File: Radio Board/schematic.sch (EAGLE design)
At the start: 3 parts, among them U1 XBP9X-DMRS-001

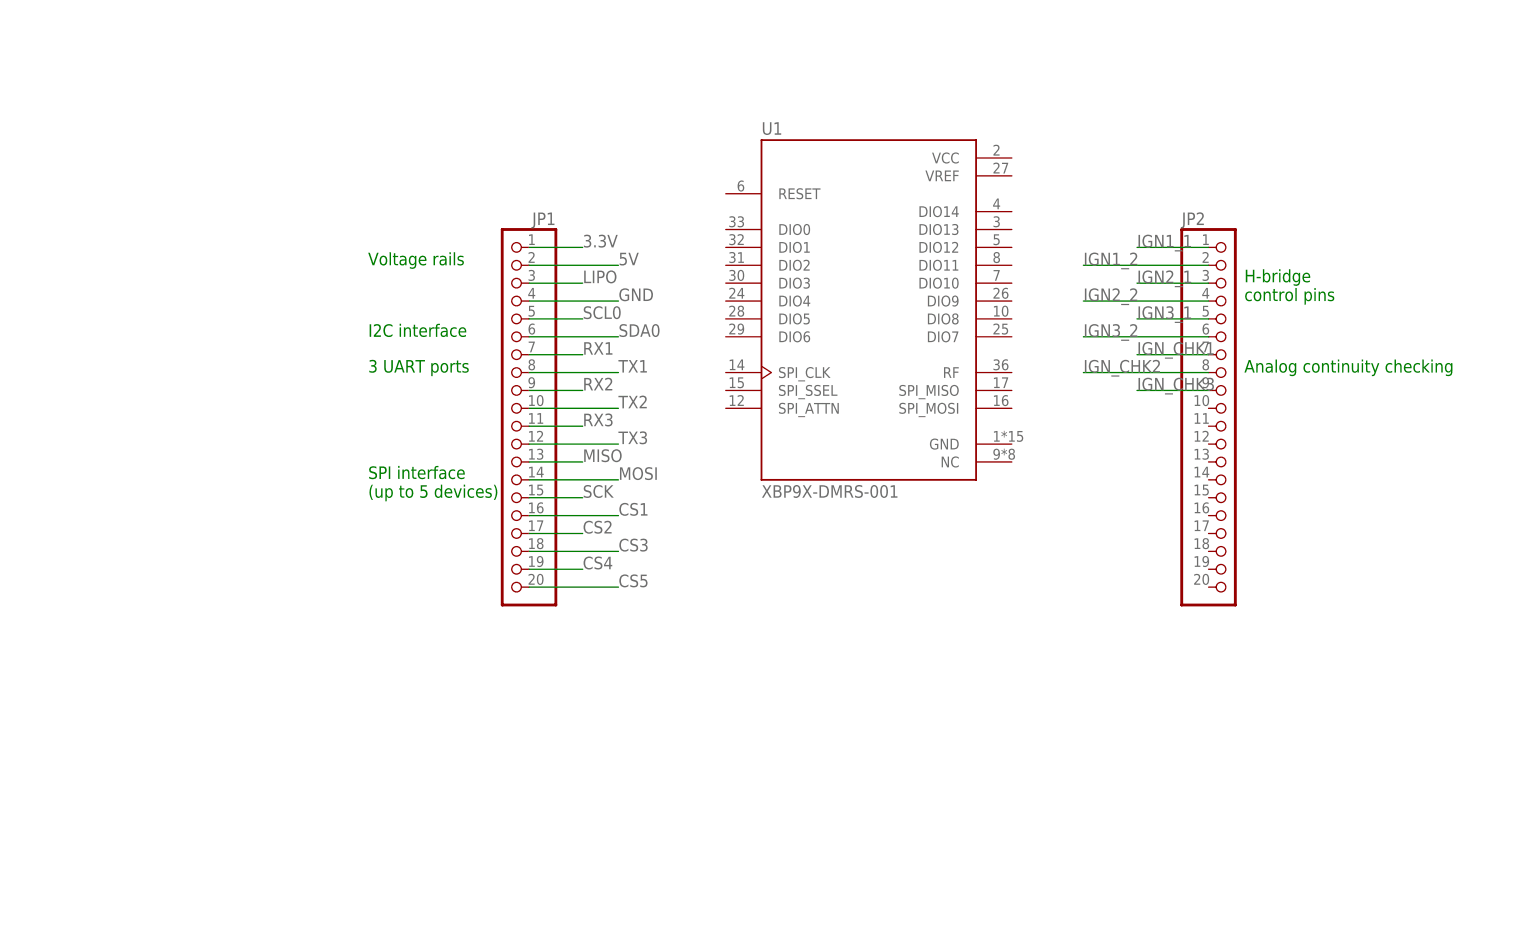
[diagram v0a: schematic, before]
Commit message: Added GPS module and complementary components
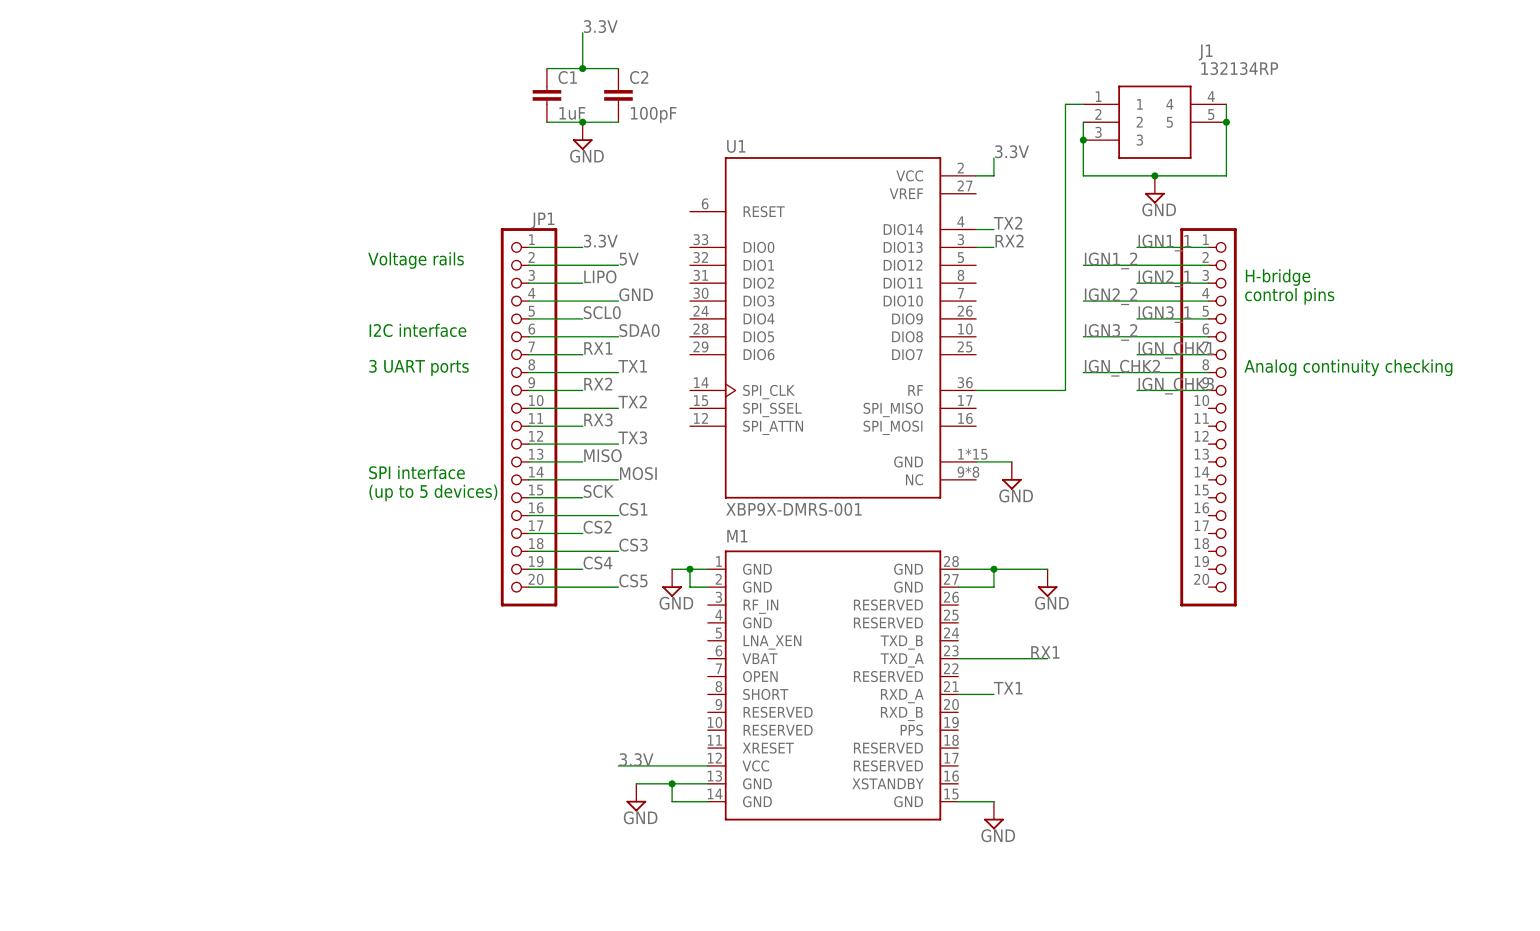
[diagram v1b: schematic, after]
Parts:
- added C1: 1uF, SparkFun-Capacitors:0.1UF-0603-100V-10%
- added C2: 100pF, SparkFun-Capacitors:0.1UF-0603-100V-10%
- added J1: 132134RP, 132134RP:132134RP
- added M1: (no value), trimble:COPERNICUS-II-SMD
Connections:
- new net N$1: J1.1, U1.RF
- net 3.3V: now also C1.1, C2.1, M1.VCC, U1.VCC
- net GND: now also C1.2, C2.2, J1.2, J1.3, J1.4, J1.5, M1.GND@1, M1.GND@13, M1.GND@14, M1.GND@15, M1.GND@2, M1.GND@27, M1.GND@28, U1.GND
- net RX1: now also M1.TXD_A
- net RX2: now also U1.DIO13
- net TX1: now also M1.RXD_A
- net TX2: now also U1.DIO14
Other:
- moved on the sheet: U1

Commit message: Finished wiring
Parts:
- removed M1: (no value), trimble:COPERNICUS-II-SMD
- added GPS, J3: (no value), SparkFun-Connectors:CONN_10NO_SILK_PTH_FEMALE
- renumbered U1 to RADIO
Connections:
- net 3.3V: now also J3.8; no longer M1.VCC
- net GND: now also J3.9; no longer M1.GND@1, M1.GND@13, M1.GND@14, M1.GND@15, M1.GND@2, M1.GND@27, M1.GND@28
- net RX1: now also GPS.7; no longer M1.TXD_A
- net TX1: now also GPS.5; no longer M1.RXD_A
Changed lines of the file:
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@@
 <layer number="154" name="FabDoc2" color="2" fill="1" visible="no" active="no"/>
 <layer number="155" name="FabDoc3" color="7" fill="15" visible="no" active="no"/>
+<layer number="156" name="gesam-Maß" color="7" fill="1" visible="no" active="no"/>
+<layer number="157" name="FaceMchng" color="7" fill="1" visible="no" active="no"/>
+<layer number="158" name="FaceMMeas" color="7" fill="1" visible="no" active="no"/>
+<layer number="159" name="Geh-Bear2" color="7" fill="1" visible="no" active="no"/>
+<layer number="160" name="Topologie" color="7" fill="1" visible="no" active="no"/>
+<layer number="161" name="tomplace2" color="7" fill="1" visible="no" active="no"/>
 <layer number="166" name="AntennaArea" color="7" fill="1" visible="no" active="no"/>
 <layer number="168" name="4mmHeightArea" color="7" fill="1" visible="no" active="no"/>
@@
 <layer number="250" name="Descript" color="7" fill="1" visible="no" active="no"/>
 <layer number="251" name="SMDround" color="7" fill="1" visible="no" active="no"/>
+<layer number="252" name="BR-BS" color="7" fill="1" visible="no" active="no"/>
 <layer number="253" name="Extra" color="7" fill="1" visible="no" active="no"/>
 <layer number="254" name="cooling" color="7" fill="1" visible="no" active="yes"/>
@@
 <part name="JP1" library="adafruit" library_urn="urn:adsk.eagle:library:420" deviceset="PINHD-1X20" device="" package3d_urn="urn:adsk.eagle:package:6240777/1"/>
 <part name="JP2" library="adafruit" library_urn="urn:adsk.eagle:library:420" deviceset="PINHD-1X20" device="" package3d_urn="urn:adsk.eagle:package:6240777/1"/>
-<part name="U1" library="XBP9X-DMRS-001" deviceset="XBP9X-DMRS-001" device=""/>
+<part name="RADIO" library="XBP9X-DMRS-001" deviceset="XBP9X-DMRS-001" device=""/>
 <part name="C1" library="SparkFun-Capacitors" deviceset="0.1UF" device="-0603-100V-10%" value="1uF"/>
 <part name="C2" library="SparkFun-Capacitors" deviceset="0.1UF" device="-0603-100V-10%" value="100pF"/>
@@
 <part name="SUPPLY3" library="supply2" library_urn="urn:adsk.eagle:library:372" deviceset="GND" device=""/>
 <part name="SUPPLY1" library="supply2" library_urn="urn:adsk.eagle:library:372" deviceset="GND" device=""/>
-<part name="M1" library="trimble" library_urn="urn:adsk.eagle:library:404" deviceset="COPERNICUS-II" device="-SMD" package3d_urn="urn:adsk.eagle:package:30197/1"/>
-<part name="SUPPLY4" library="supply2" library_urn="urn:adsk.eagle:library:372" deviceset="GND" device=""/>
-<part name="SUPPLY5" library="supply2" library_urn="urn:adsk.eagle:library:372" deviceset="GND" device=""/>
-<part name="SUPPLY6" library="supply2" library_urn="urn:adsk.eagle:library:372" deviceset="GND" device=""/>
-<part name="SUPPLY7" library="supply2" library_urn="urn:adsk.eagle:library:372" deviceset="GND" device=""/>
+<part name="GPS" library="SparkFun-Connectors" deviceset="CONN_10" device="NO_SILK_PTH_FEMALE"/>
+<part name="J3" library="SparkFun-Connectors" deviceset="CONN_10" device="NO_SILK_PTH_FEMALE"/>
 </parts>
 <sheets>
@@
 <attribute name="VALUE" x="125.73" y="20.32" size="1.778" layer="96"/>
 </instance>
-<instance part="U1" gate="G$1" x="76.2" y="63.5" smashed="yes">
+<instance part="RADIO" gate="G$1" x="76.2" y="63.5" smashed="yes">
 <attribute name="NAME" x="60.96" y="87.122" size="1.778" layer="95"/>
 <attribute name="VALUE" x="60.96" y="37.338" size="1.778" layer="96" align="top-left"/>
@@
 <attribute name="VALUE" x="99.695" y="37.465" size="1.778" layer="96"/>
 </instance>
-<instance part="M1" gate="G$1" x="76.2" y="10.16" smashed="yes">
-<attribute name="NAME" x="60.96" y="31.75" size="1.778" layer="95"/>
-<attribute name="VALUE" x="60.96" y="-10.16" size="1.778" layer="96"/>
-</instance>
-<instance part="SUPPLY4" gate="GND" x="106.68" y="25.4" smashed="yes">
-<attribute name="VALUE" x="104.775" y="22.225" size="1.778" layer="96"/>
-</instance>
-<instance part="SUPPLY5" gate="GND" x="53.34" y="25.4" smashed="yes">
-<attribute name="VALUE" x="51.435" y="22.225" size="1.778" layer="96"/>
-</instance>
-<instance part="SUPPLY6" gate="GND" x="48.26" y="-5.08" smashed="yes">
-<attribute name="VALUE" x="46.355" y="-8.255" size="1.778" layer="96"/>
-</instance>
-<instance part="SUPPLY7" gate="GND" x="99.06" y="-7.62" smashed="yes">
-<attribute name="VALUE" x="97.155" y="-10.795" size="1.778" layer="96"/>
+<instance part="GPS" gate="J1" x="60.96" y="20.32" smashed="yes">
+<attribute name="VALUE" x="60.96" y="-2.286" size="1.778" layer="96" font="vector"/>
+<attribute name="NAME" x="60.96" y="28.448" size="1.778" layer="95" font="vector"/>
+</instance>
+<instance part="J3" gate="J1" x="99.06" y="7.62" smashed="yes" rot="R180">
+<attribute name="VALUE" x="99.06" y="30.226" size="1.778" layer="96" font="vector" rot="R180"/>
+<attribute name="NAME" x="99.06" y="-0.508" size="1.778" layer="95" font="vector" rot="R180"/>
 </instance>
 </instances>
@@
 </segment>
 <segment>
-<pinref part="U1" gate="G$1" pin="VCC"/>
+<pinref part="RADIO" gate="G$1" pin="VCC"/>
 <wire x1="99.06" y1="83.82" x2="96.52" y2="83.82" width="0.1524" layer="91"/>
 <wire x1="99.06" y1="83.82" x2="99.06" y2="86.36" width="0.1524" layer="91"/>
@@
 </segment>
 <segment>
-<pinref part="M1" gate="G$1" pin="VCC"/>
-<wire x1="58.42" y1="0" x2="45.72" y2="0" width="0.1524" layer="91"/>
-<label x="45.72" y="0" size="1.778" layer="95"/>
+<pinref part="J3" gate="J1" pin="8"/>
+<wire x1="88.9" y1="7.62" x2="76.2" y2="7.62" width="0.1524" layer="91"/>
+<wire x1="76.2" y1="7.62" x2="76.2" y2="-2.54" width="0.1524" layer="91"/>
+<label x="76.2" y="-2.54" size="1.778" layer="95"/>
 </segment>
 </net>
@@
 </segment>
 <segment>
-<pinref part="U1" gate="G$1" pin="GND"/>
+<pinref part="RADIO" gate="G$1" pin="GND"/>
 <pinref part="SUPPLY1" gate="GND" pin="GND"/>
 <wire x1="96.52" y1="43.18" x2="101.6" y2="43.18" width="0.1524" layer="91"/>
 </segment>
 <segment>
-<pinref part="SUPPLY5" gate="GND" pin="GND"/>
-<pinref part="M1" gate="G$1" pin="GND@1"/>
-<wire x1="53.34" y1="27.94" x2="55.88" y2="27.94" width="0.1524" layer="91"/>
-<pinref part="M1" gate="G$1" pin="GND@2"/>
-<wire x1="55.88" y1="27.94" x2="58.42" y2="27.94" width="0.1524" layer="91"/>
-<wire x1="58.42" y1="25.4" x2="55.88" y2="25.4" width="0.1524" layer="91"/>
-<wire x1="55.88" y1="25.4" x2="55.88" y2="27.94" width="0.1524" layer="91"/>
-<junction x="55.88" y="27.94"/>
-</segment>
-<segment>
-<pinref part="M1" gate="G$1" pin="GND@28"/>
-<pinref part="SUPPLY4" gate="GND" pin="GND"/>
-<wire x1="93.98" y1="27.94" x2="99.06" y2="27.94" width="0.1524" layer="91"/>
-<pinref part="M1" gate="G$1" pin="GND@27"/>
-<wire x1="99.06" y1="27.94" x2="106.68" y2="27.94" width="0.1524" layer="91"/>
-<wire x1="93.98" y1="25.4" x2="99.06" y2="25.4" width="0.1524" layer="91"/>
-<wire x1="99.06" y1="25.4" x2="99.06" y2="27.94" width="0.1524" layer="91"/>
-<junction x="99.06" y="27.94"/>
-</segment>
-<segment>
-<pinref part="M1" gate="G$1" pin="GND@15"/>
-<pinref part="SUPPLY7" gate="GND" pin="GND"/>
-<wire x1="93.98" y1="-5.08" x2="99.06" y2="-5.08" width="0.1524" layer="91"/>
-</segment>
-<segment>
-<pinref part="M1" gate="G$1" pin="GND@13"/>
-<pinref part="SUPPLY6" gate="GND" pin="GND"/>
-<wire x1="58.42" y1="-2.54" x2="53.34" y2="-2.54" width="0.1524" layer="91"/>
-<pinref part="M1" gate="G$1" pin="GND@14"/>
-<wire x1="53.34" y1="-2.54" x2="48.26" y2="-2.54" width="0.1524" layer="91"/>
-<wire x1="58.42" y1="-5.08" x2="53.34" y2="-5.08" width="0.1524" layer="91"/>
-<wire x1="53.34" y1="-5.08" x2="53.34" y2="-2.54" width="0.1524" layer="91"/>
-<junction x="53.34" y="-2.54"/>
+<pinref part="J3" gate="J1" pin="9"/>
+<wire x1="88.9" y1="5.08" x2="86.36" y2="5.08" width="0.1524" layer="91"/>
+<wire x1="86.36" y1="5.08" x2="86.36" y2="-5.08" width="0.1524" layer="91"/>
+<label x="86.36" y="-5.08" size="1.778" layer="95"/>
 </segment>
 </net>
@@
 </segment>
 <segment>
-<pinref part="M1" gate="G$1" pin="TXD_A"/>
-<wire x1="93.98" y1="15.24" x2="106.68" y2="15.24" width="0.1524" layer="91"/>
-<label x="104.14" y="15.24" size="1.778" layer="95"/>
+<pinref part="GPS" gate="J1" pin="7"/>
+<wire x1="71.12" y1="17.78" x2="78.74" y2="17.78" width="0.1524" layer="91"/>
+<label x="73.66" y="17.78" size="1.778" layer="95"/>
 </segment>
 </net>
@@
 </segment>
 <segment>
-<pinref part="M1" gate="G$1" pin="RXD_A"/>
-<wire x1="93.98" y1="10.16" x2="99.06" y2="10.16" width="0.1524" layer="91"/>
-<label x="99.06" y="10.16" size="1.778" layer="95"/>
+<pinref part="GPS" gate="J1" pin="5"/>
+<wire x1="71.12" y1="12.7" x2="81.28" y2="12.7" width="0.1524" layer="91"/>
+<label x="76.2" y="12.7" size="1.778" layer="95"/>
 </segment>
 </net>
@@
 </segment>
 <segment>
-<pinref part="U1" gate="G$1" pin="DIO13"/>
+<pinref part="RADIO" gate="G$1" pin="DIO13"/>
 <wire x1="96.52" y1="73.66" x2="99.06" y2="73.66" width="0.1524" layer="91"/>
 <label x="99.06" y="73.66" size="1.778" layer="95"/>
@@
 </segment>
 <segment>
-<pinref part="U1" gate="G$1" pin="DIO14"/>
+<pinref part="RADIO" gate="G$1" pin="DIO14"/>
 <wire x1="96.52" y1="76.2" x2="99.06" y2="76.2" width="0.1524" layer="91"/>
 <label x="99.06" y="76.2" size="1.778" layer="95"/>
@@
 <net name="N$1" class="0">
 <segment>
-<pinref part="U1" gate="G$1" pin="RF"/>
+<pinref part="RADIO" gate="G$1" pin="RF"/>
 <wire x1="96.52" y1="53.34" x2="109.22" y2="53.34" width="0.1524" layer="91"/>
 <wire x1="109.22" y1="53.34" x2="109.22" y2="93.98" width="0.1524" layer="91"/>

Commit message: Finished Routing
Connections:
- net N$1 renamed RF
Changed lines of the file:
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@@
 </segment>
 </net>
-<net name="N$1" class="0">
+<net name="RF" class="0">
 <segment>
 <pinref part="RADIO" gate="G$1" pin="RF"/>
@@
 </sheet>
 </sheets>
+<errors>
+</errors>
 </schematic>
 </drawing>

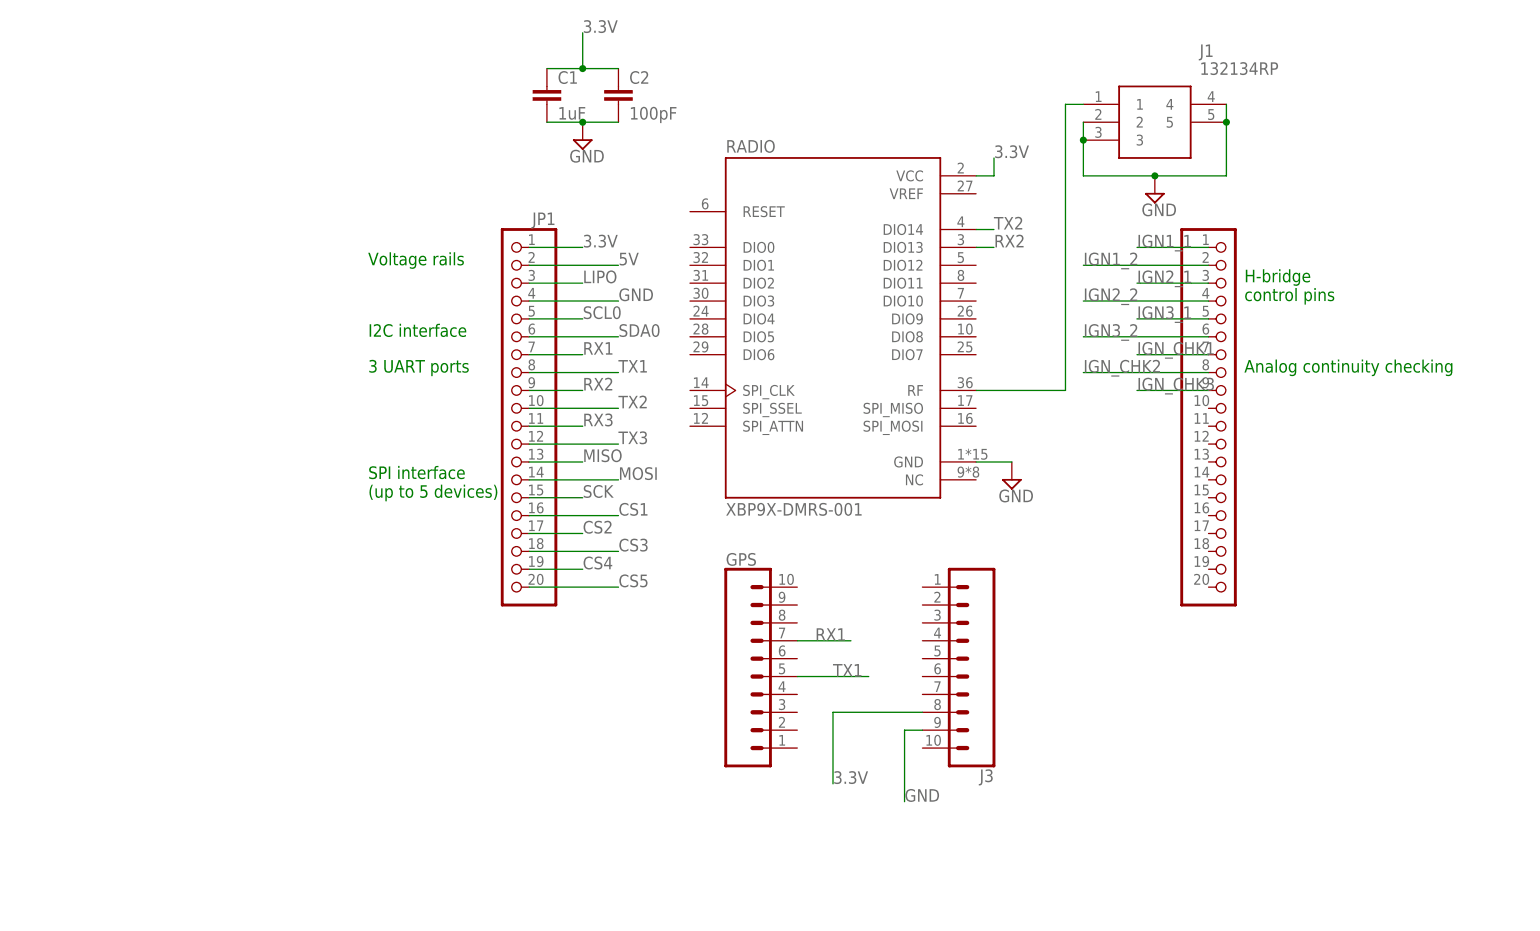
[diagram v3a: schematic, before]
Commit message: Updated radio & GPS
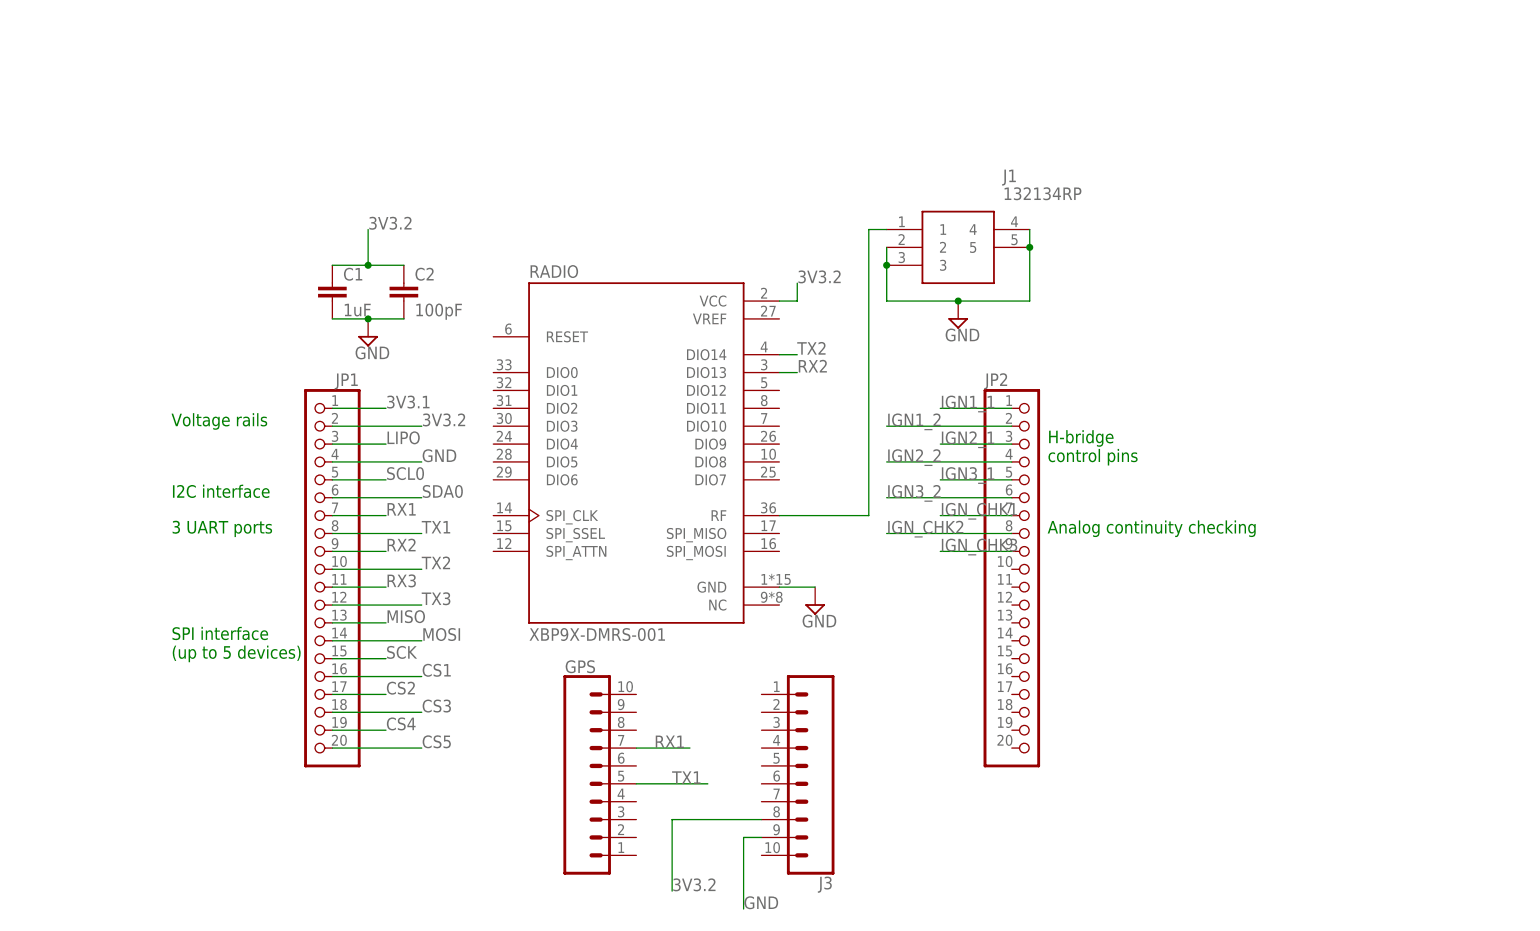
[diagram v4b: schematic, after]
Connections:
- removed net 3.3V: C1.1, C2.1, J3.8, JP1.1, RADIO.VCC
- removed net 5V: JP1.2
- new net 3V3.1: JP1.1
- new net 3V3.2: C1.1, C2.1, J3.8, JP1.2, RADIO.VCC
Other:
- moved on the sheet: C1, C2, GPS, J1, J3, JP1, RADIO
